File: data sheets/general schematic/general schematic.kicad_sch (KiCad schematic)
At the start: 5 parts, among them U1 Pico

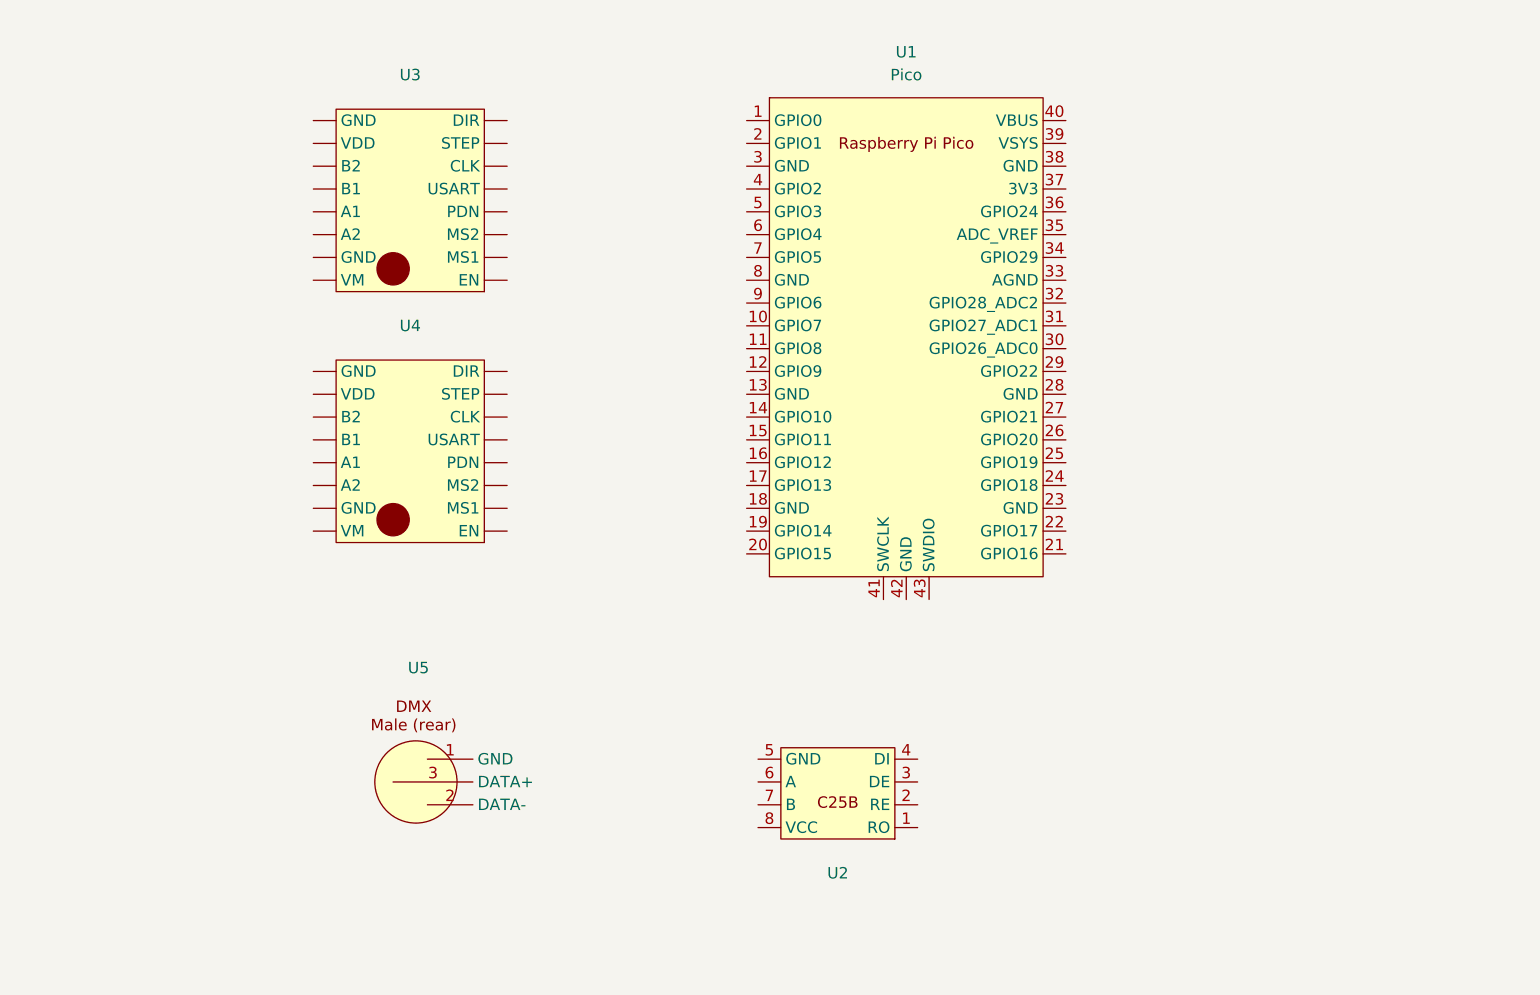
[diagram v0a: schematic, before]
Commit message: adjusted pin connections + finished schematics
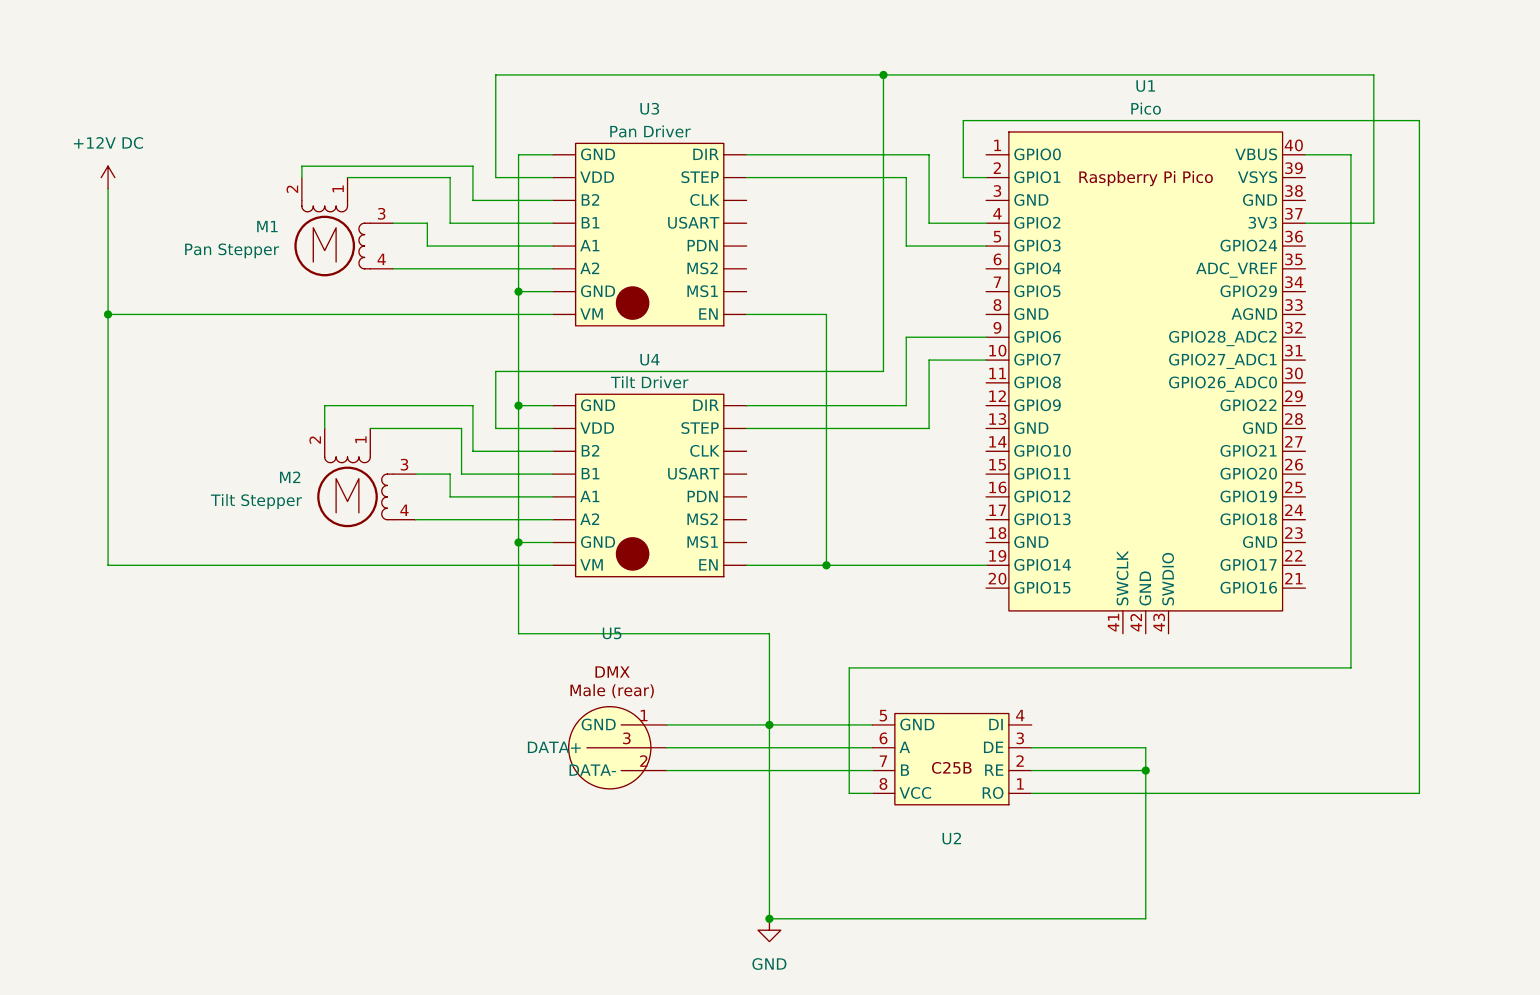
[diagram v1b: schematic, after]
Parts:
- added M1: Pan Stepper, symbol Motor:Stepper_Motor_bipolar
- added M2: Tilt Stepper, symbol Motor:Stepper_Motor_bipolar
- U3: value ~ -> Pan Driver
- U4: value ~ -> Tilt Driver
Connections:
- net GND: now reaches U4. (VM)
- net GND: now also U2.2 (RE), U2.3 (DE), U2.5 (GND), U3. (VM), U5.1 (GND)
- net at U5.2 (DATA-): now also U2.7 (B)
- net at U5.3 (DATA+): now also U2.6 (A)
- net at U1.10 (GPIO7): now also U4. (VM)
- net at U1.19 (GPIO14): now also U3. (VM), U4. (VM)
- net at U1.2 (GPIO1): now also U2.1 (RO)
- net at U1.37 (3V3): now also U3. (VM), U4. (VM)
- net at U1.4 (GPIO2): now also U3. (VM)
- net at U1.40 (VBUS): now also U2.8 (VCC)
- net at U1.5 (GPIO3): now also U3. (VM)
- net at U1.9 (GPIO6): now also U4. (VM)
- new net: M2.1, U4. (VM)
- new net: M2.2 (-), U4. (VM)
- new net: M2.3, U4. (VM)
- new net: M2.4, U4. (VM)
- new net: M1.1, U3. (VM)
- new net: M1.2 (-), U3. (VM)
- new net: M1.3, U3. (VM)
- new net: M1.4, U3. (VM)
- new net +12V DC: U3. (VM), U4. (VM)
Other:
- moved on the sheet: U1, U2, U3, U4

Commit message: updated schematics
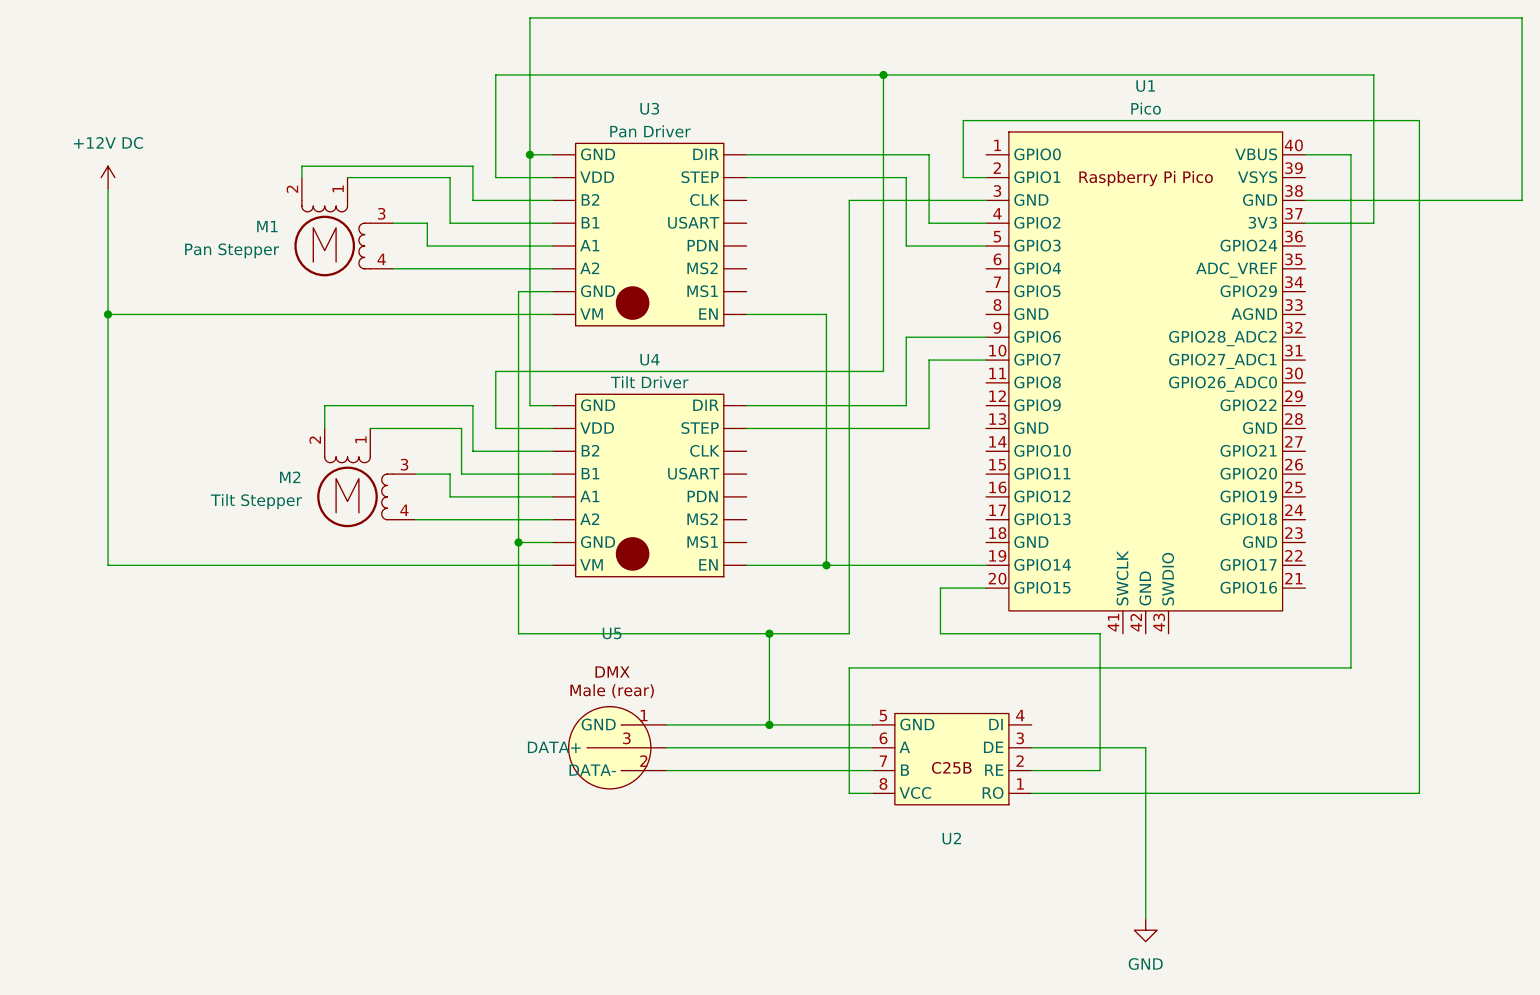
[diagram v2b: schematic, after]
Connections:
- net GND: no longer U2.2 (RE), U2.5 (GND), U3. (VM), U4. (VM), U5.1 (GND)
- net at U1.20 (GPIO15): now also U2.2 (RE)
- net at U1.3 (GND): now also U2.5 (GND), U3. (VM), U4. (VM), U5.1 (GND)
- net at U1.38 (GND): now also U3. (VM), U4. (VM)
- new net: U1.19 (GPIO14), U3. (VM), U4. (VM)
- new net: U1.37 (3V3), U3. (VM), U4. (VM)
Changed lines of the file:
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@@
-	)
-	(junction
-		(at 107.95 88.9)
-		(diameter 0)
-		(color 0 0 0 0)
-	)
-	(junction
-		(at 107.95 76.2)
-		(diameter 0)
-		(color 0 0 0 0)
 	)
 	(junction
@@
 	)
 	(junction
-		(at 135.89 146.05)
-		(diameter 0)
-		(color 0 0 0 0)
-	)
-	(junction
 		(at 135.89 124.46)
 		(diameter 0)
@@
 	)
 	(junction
-		(at 177.8 129.54)
+		(at 109.22 60.96)
 		(diameter 0)
 		(color 0 0 0 0)
 	)
+	(junction
+		(at 135.89 114.3)
+		(diameter 0)
+		(color 0 0 0 0)
+	)
 	(wire
 		(pts
@@
 	(wire
 		(pts
+			(xy 109.22 60.96) (xy 109.22 88.9)
+		)
+		(stroke
+			(width 0)
+			(type default)
+		)
+	)
+	(wire
+		(pts
 			(xy 124.46 129.54) (xy 147.32 129.54)
 		)
@@
 	(wire
 		(pts
-			(xy 165.1 129.54) (xy 177.8 129.54)
-		)
-		(stroke
-			(width 0)
-			(type default)
-		)
-	)
-	(wire
-		(pts
 			(xy 96.52 96.52) (xy 100.33 96.52)
 		)
@@
 	(wire
 		(pts
+			(xy 219.71 45.72) (xy 219.71 66.04)
+		)
+		(stroke
+			(width 0)
+			(type default)
+		)
+	)
+	(wire
+		(pts
+			(xy 165.1 129.54) (xy 172.72 129.54)
+		)
+		(stroke
+			(width 0)
+			(type default)
+		)
+	)
+	(wire
+		(pts
 			(xy 200.66 60.96) (xy 195.58 60.96)
 		)
@@
 	(wire
 		(pts
+			(xy 135.89 114.3) (xy 144.78 114.3)
+		)
+		(stroke
+			(width 0)
+			(type default)
+		)
+	)
+	(wire
+		(pts
 			(xy 93.98 73.66) (xy 111.76 73.66)
 		)
@@
 	(wire
 		(pts
+			(xy 144.78 66.04) (xy 160.02 66.04)
+		)
+		(stroke
+			(width 0)
+			(type default)
+		)
+	)
+	(wire
+		(pts
 			(xy 133.35 91.44) (xy 153.67 91.44)
 		)
@@
 	(wire
 		(pts
+			(xy 144.78 114.3) (xy 144.78 66.04)
+		)
+		(stroke
+			(width 0)
+			(type default)
+		)
+	)
+	(wire
+		(pts
 			(xy 124.46 124.46) (xy 135.89 124.46)
 		)
@@
 	(wire
 		(pts
-			(xy 107.95 88.9) (xy 111.76 88.9)
+			(xy 219.71 66.04) (xy 195.58 66.04)
 		)
 		(stroke
@@
 	(wire
 		(pts
-			(xy 107.95 60.96) (xy 107.95 76.2)
-		)
-		(stroke
-			(width 0)
-			(type default)
-		)
-	)
-	(wire
-		(pts
 			(xy 133.35 60.96) (xy 153.67 60.96)
 		)
@@
 	(wire
 		(pts
+			(xy 172.72 114.3) (xy 154.94 114.3)
+		)
+		(stroke
+			(width 0)
+			(type default)
+		)
+	)
+	(wire
+		(pts
 			(xy 200.66 118.11) (xy 200.66 60.96)
 		)
@@
 	(wire
 		(pts
+			(xy 109.22 45.72) (xy 219.71 45.72)
+		)
+		(stroke
+			(width 0)
+			(type default)
+		)
+	)
+	(wire
+		(pts
 			(xy 142.24 106.68) (xy 160.02 106.68)
 		)
@@
 	(wire
 		(pts
-			(xy 107.95 88.9) (xy 107.95 104.14)
+			(xy 154.94 109.22) (xy 160.02 109.22)
+		)
+		(stroke
+			(width 0)
+			(type default)
+		)
+	)
+	(wire
+		(pts
+			(xy 111.76 88.9) (xy 109.22 88.9)
+		)
+		(stroke
+			(width 0)
+			(type default)
+		)
+	)
+	(wire
+		(pts
+			(xy 107.95 76.2) (xy 107.95 104.14)
 		)
 		(stroke
@@
 	(wire
 		(pts
-			(xy 177.8 146.05) (xy 135.89 146.05)
-		)
-		(stroke
-			(width 0)
-			(type default)
-		)
-	)
-	(wire
-		(pts
-			(xy 177.8 129.54) (xy 177.8 146.05)
+			(xy 177.8 127) (xy 177.8 146.05)
 		)
 		(stroke
@@
 	(wire
 		(pts
-			(xy 111.76 60.96) (xy 107.95 60.96)
-		)
-		(stroke
-			(width 0)
-			(type default)
-		)
-	)
-	(wire
-		(pts
-			(xy 135.89 146.05) (xy 135.89 124.46)
+			(xy 111.76 60.96) (xy 109.22 60.96)
 		)
 		(stroke
@@
 	(wire
 		(pts
+			(xy 109.22 60.96) (xy 109.22 45.72)
+		)
+		(stroke
+			(width 0)
+			(type default)
+		)
+	)
+	(wire
+		(pts
 			(xy 203.2 68.58) (xy 195.58 68.58)
 		)
@@
 	(wire
 		(pts
-			(xy 177.8 127) (xy 177.8 129.54)
-		)
-		(stroke
-			(width 0)
-			(type default)
-		)
-	)
-	(wire
-		(pts
-			(xy 107.95 76.2) (xy 107.95 88.9)
+			(xy 154.94 114.3) (xy 154.94 109.22)
 		)
 		(stroke
@@
 	(wire
 		(pts
+			(xy 172.72 129.54) (xy 172.72 114.3)
+		)
+		(stroke
+			(width 0)
+			(type default)
+		)
+	)
+	(wire
+		(pts
 			(xy 144.78 118.11) (xy 200.66 118.11)
 		)
@@
 	)
 	(symbol
-		(lib_name "theatre_mover_libraries:TMC_2209_driver")
 		(lib_id "theatre_mover_libraries:TMC_2209_driver")
 		(at 121.92 97.79 180)
@@
 	)
 	(symbol
+		(lib_id "power:GND")
+		(at 177.8 146.05 0)
+		(unit 1)
+		(exclude_from_sim no)
+		(in_bom yes)
+		(on_board yes)
+		(dnp no)
+		(fields_autoplaced yes)
+		(property "Reference" "#PWR02"
+			(at 177.8 152.4 0)
+			(effects
+				(font
+					(size 1.27 1.27)
+				)
+				(hide yes)
+			)
+		)
+		(property "Value" "GND"
+			(at 177.8 151.13 0)
+			(effects
+				(font
+					(size 1.27 1.27)
+				)
+			)
+		)
+		(property "Footprint" ""
+			(at 177.8 146.05 0)
+			(effects
+				(font
+					(size 1.27 1.27)
+				)
+				(hide yes)
+			)
+		)
+		(property "Datasheet" ""
+			(at 177.8 146.05 0)
+			(effects
+				(font
+					(size 1.27 1.27)
+				)
+				(hide yes)
+			)
+		)
+		(property "Description" "Power symbol creates a global label with name \"GND\" , ground"
+			(at 177.8 146.05 0)
+			(effects
+				(font
+					(size 1.27 1.27)
+				)
+				(hide yes)
+			)
+		)
+		(pin "1"
+		)
+		(instances
+			(project "general schematic"
+				(path "/c8441d39-2320-49bb-a776-18a150583cfc"
+					(reference "#PWR02")
+					(unit 1)
+				)
+			)
+		)
+	)
+	(symbol
 		(lib_id "MCU_RaspberryPi_and_Boards:Pico")
 		(at 177.8 85.09 0)
@@
 	)
 	(symbol
-		(lib_name "theatre_mover_libraries:TMC_2209_driver")
 		(lib_id "theatre_mover_libraries:TMC_2209_driver")
 		(at 121.92 69.85 180)
@@
 					(unit 1)
 				)
-			)
-		)
-	)
-	(symbol
-		(lib_id "power:GND")
-		(at 135.89 146.05 0)
-		(unit 1)
-		(exclude_from_sim no)
-		(in_bom yes)
-		(on_board yes)
-		(dnp no)
-		(fields_autoplaced yes)
-		(property "Reference" "#PWR06"
-			(at 135.89 152.4 0)
-			(effects
-				(font
-					(size 1.27 1.27)
-				)
-				(hide yes)
-			)
-		)
-		(property "Value" "GND"
-			(at 135.89 151.13 0)
-			(effects
-				(font
-					(size 1.27 1.27)
-				)
-			)
-		)
-		(property "Footprint" ""
-			(at 135.89 146.05 0)
-			(effects
-				(font
-					(size 1.27 1.27)
-				)
-				(hide yes)
-			)
-		)
-		(property "Datasheet" ""
-			(at 135.89 146.05 0)
-			(effects
-				(font
-					(size 1.27 1.27)
-				)
-				(hide yes)
-			)
-		)
-		(property "Description" "Power symbol creates a global label with name \"GND\" , ground"
-			(at 135.89 146.05 0)
-			(effects
-				(font
-					(size 1.27 1.27)
-				)
-				(hide yes)
-			)
-		)
-		(pin "1"
-		)
-		(instances
-			(project "general schematic"
-				(path "/c8441d39-2320-49bb-a776-18a150583cfc"
-					(reference "#PWR06")
-					(unit 1)
-				)

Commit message: *project reboot!* reinstall drivers and fixed mover.run_towards function
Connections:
- net GND: now also U3. (VM), U4. (VM)
- net at U1.3 (GND), U2.5 (GND), U5.1 (GND): no longer U3. (VM), U4. (VM)
- new net: U1.19 (GPIO14), U3. (VM), U4. (VM)
- new net: U1.37 (3V3), U3. (VM), U4. (VM)
- new net: U1.38 (GND), U3. (VM), U4. (VM)
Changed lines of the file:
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@@
-	)
-	(junction
-		(at 107.95 104.14)
-		(diameter 0)
-		(color 0 0 0 0)
 	)
 	(junction
@@
 	)
 	(junction
-		(at 135.89 114.3)
+		(at 68.58 104.14)
 		(diameter 0)
 		(color 0 0 0 0)
@@
 	(wire
 		(pts
-			(xy 107.95 104.14) (xy 107.95 114.3)
+			(xy 54.61 114.3) (xy 54.61 64.77)
+		)
+		(stroke
+			(width 0)
+			(type default)
+		)
+	)
+	(wire
+		(pts
+			(xy 68.58 104.14) (xy 68.58 114.3)
 		)
 		(stroke
@@
 	(wire
 		(pts
+			(xy 68.58 114.3) (xy 54.61 114.3)
+		)
+		(stroke
+			(width 0)
+			(type default)
+		)
+	)
+	(wire
+		(pts
 			(xy 62.23 78.74) (xy 62.23 106.68)
 		)
@@
 	(wire
 		(pts
-			(xy 107.95 104.14) (xy 111.76 104.14)
-		)
-		(stroke
-			(width 0)
-			(type default)
-		)
-	)
-	(wire
-		(pts
 			(xy 97.79 68.58) (xy 97.79 71.12)
 		)
@@
 	(wire
 		(pts
-			(xy 107.95 114.3) (xy 135.89 114.3)
-		)
-		(stroke
-			(width 0)
-			(type default)
-		)
-	)
-	(wire
-		(pts
 			(xy 97.79 71.12) (xy 111.76 71.12)
 		)
@@
 	(wire
 		(pts
+			(xy 68.58 104.14) (xy 111.76 104.14)
+		)
+		(stroke
+			(width 0)
+			(type default)
+		)
+	)
+	(wire
+		(pts
 			(xy 133.35 60.96) (xy 153.67 60.96)
 		)
@@
 	(wire
 		(pts
-			(xy 107.95 76.2) (xy 107.95 104.14)
+			(xy 68.58 76.2) (xy 68.58 104.14)
 		)
 		(stroke
@@
 	(wire
 		(pts
-			(xy 107.95 76.2) (xy 111.76 76.2)
+			(xy 68.58 76.2) (xy 111.76 76.2)
 		)
 		(stroke
@@
 		)
 	)
+	(symbol
+		(lib_id "power:GND")
+		(at 54.61 64.77 180)
+		(unit 1)
+		(exclude_from_sim no)
+		(in_bom yes)
+		(on_board yes)
+		(dnp no)
+		(fields_autoplaced yes)
+		(property "Reference" "#PWR03"
+			(at 54.61 58.42 0)
+			(effects
+				(font
+					(size 1.27 1.27)
+				)
+				(hide yes)
+			)
+		)
+		(property "Value" "GND"
+			(at 54.61 59.69 0)
+			(effects
+				(font
+					(size 1.27 1.27)
+				)
+			)
+		)
+		(property "Footprint" ""
+			(at 54.61 64.77 0)
+			(effects
+				(font
+					(size 1.27 1.27)
+				)
+				(hide yes)
+			)
+		)
+		(property "Datasheet" ""
+			(at 54.61 64.77 0)
+			(effects
+				(font
+					(size 1.27 1.27)
+				)
+				(hide yes)
+			)
+		)
+		(property "Description" "Power symbol creates a global label with name \"GND\" , ground"
+			(at 54.61 64.77 0)
+			(effects
+				(font
+					(size 1.27 1.27)
+				)
+				(hide yes)
+			)
+		)
+		(pin "1"
+		)
+		(instances
+			(project "general schematic"
+				(path "/c8441d39-2320-49bb-a776-18a150583cfc"
+					(reference "#PWR03")
+					(unit 1)
+				)
+			)
+		)
+	)
